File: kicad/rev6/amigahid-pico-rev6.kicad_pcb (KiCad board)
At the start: 2 copper layers, 100 x 80 mm, 115 parts, among them J1 A500 KBD OUT, J10 PS/2 KBD OUT, J11 DIN5 KBD IN, J12 PS/2 KBD IN, J13 USB-C AUX 5V, J2 DEBUG UART+SWD, J3 OLED I2C, J4 USB-A HOST, J7 SPARE GP28, J8 A500 KBD IN, J9 DIN5 KBD OUT, P1 DE9 MALE PORT 1, P2 DE9 MALE PORT 2, Q1 BSS138, Q10 BSS138, Q11 BSS138, Q12 BSS138, Q13 BSS138, Q14 BSS138, Q15 BSS138, Q16 BSS138, Q17 BSS138, Q18 BSS138, Q19 BSS138, Q2 BSS138, Q3 BSS138, Q4 BSS138, Q5 BSS138, Q6 BSS138, Q7 BSS138, Q8 BSS138, Q9 BSS138, U1 PicoW, U2 USBLC6-2SC6

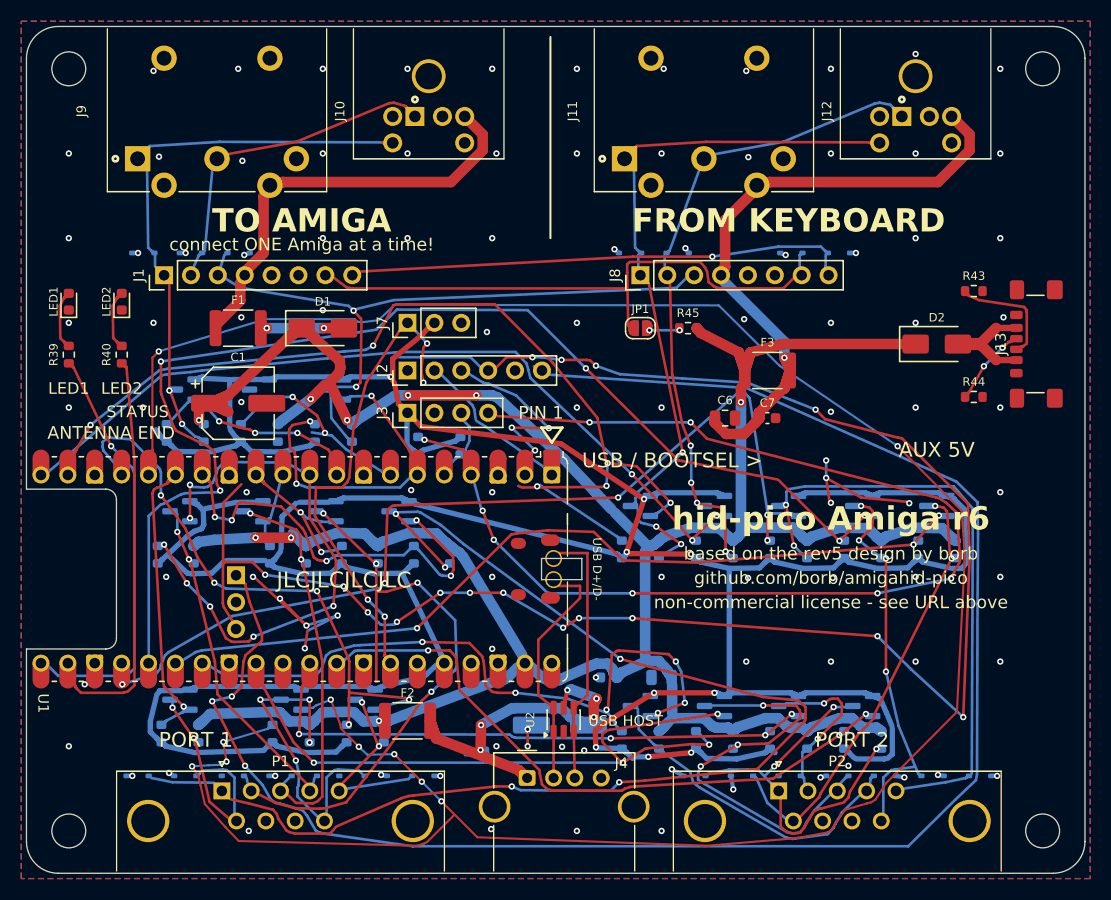
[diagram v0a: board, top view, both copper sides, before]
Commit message: kicad: drop the duplicated rev6 copper and trim the dead stubs
444 of the board's 2075 track and via objects were exact duplicates - same net, layer,
endpoints and width, stacked on top of each other by the successive re-lays.  they are
gone, which is most of the -4158 lines here.  they also explain why the last pass could
not clean up the dangling stubs: every stub had a copy of itself lying on it, so a
"does anything else touch this?" test always answered yes.

three stubs are trimmed back to their last live junction rather than deleted, because
each carries a junction partway along and deleting it - which is what the DRC line
suggests, since it reports the track's start, not its free end - orphans something:

  /cont1_h  F.Cu  11.15 -> 2.91 mm   (the remainder feeds the via on R12.2)
  /swdio    B.Cu   6.75 -> 0.29 mm
  /swdio    F.Cu   2.44 -> 0.29 mm

17 mm of unterminated copper gone.  the four sub-0.5 mm nubs left are what remains of
those tracks between their last junction and their end; they stay because trimming them
further disconnects the junction.

P2's shell tabs get the same solid zone connection P1's already have.  the two are the
same through-hole DE9 in the same pour and had no business soldering differently; the
split was accidental, not a decision.

CLAUDE.md gains a stated gate list for board commits - the old rule only covered
schematic changes, which is how a board with a failing checker reached the branch tip
unblocked - and records the pcbnew Save() footgun that strips netclass_patterns out of
the .kicad_pro.  .gitignore learns *.rpt.

what is left, honestly - all three measured this time, not assumed:

  /kbdata still will not close.  at the board's real rules (0.2 mm copper, 0.5 mm hole)
  there is no legal path at 0.02 mm resolution: Q2.3 and R4.2 share one free pocket
  whose only opening is a 0.267 mm wall on F.Cu at (15.42, 37.26), pinched between the
  /kbclock via at (14.70, 37.55) and the /SYS5V C1.1 -> R6.1 stub.  moving that stub
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
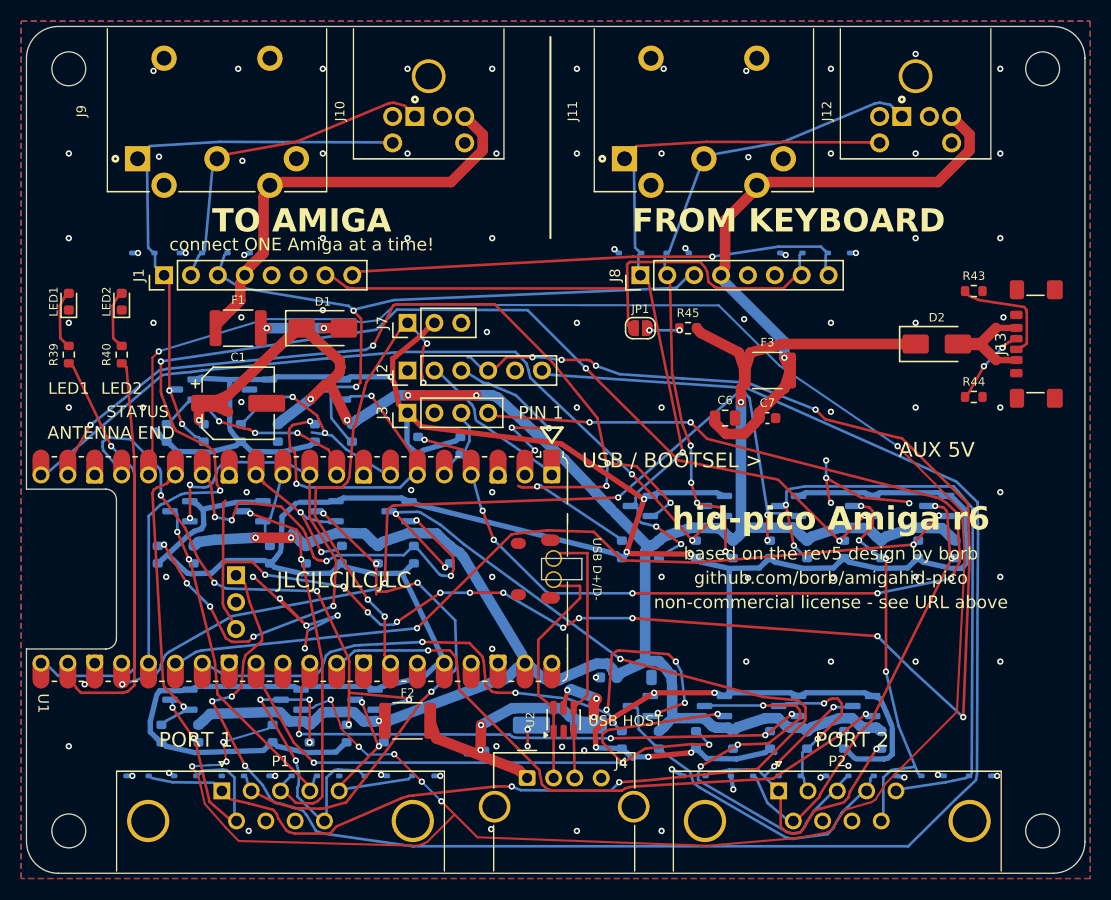
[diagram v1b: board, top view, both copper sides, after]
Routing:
- net +3V3: track 431.6 -> 349.6 mm
- net /SYS5V: track 315.3 -> 256.3 mm
- net /cont1_b1_lo: track 48.0 -> 29.4 mm
- net /cont1_h_lo: track 33.7 -> 16.7 mm
- net /gp28: track 57.8 -> 45.2 mm
- net /kbin_clk: track 78.5 -> 66.9 mm
- net /KBIN_5V: track 69.2 -> 58.6 mm
- net /swdio: track 170.7 -> 160.4 mm
- net /USBA_5V: track 40.0 -> 30.5 mm
- net /kbin_clk_lo: track 105.5 -> 96.0 mm
- net /kbclock: track 59.3 -> 50.5 mm
- net /kbreset_lo: track 38.4 -> 30.1 mm
- net /cont1_h: track 56.7 -> 48.4 mm
- net /cont1_b2_lo: track 235.6 -> 228.0 mm
- net /AMIGA_5V: track 47.5 -> 40.7 mm
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
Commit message: kicad: move the esd clamps off the de9 pins and close /kbdata
all three gates are green after this: DRC 0 violations / 0 unconnected, check_rev6_pcb
32/32, check_rev6_netlist 356/356.

the clamp rows under P1 and P2 move 0.6 mm north.  they were 0.395 mm from the DE9
through-hole pads - under JLCPCB's 0.4 mm solder-mask dam, and with no room to get an
iron onto the DE9 pins - and six of those pads' mask openings clipped a clamp body
outline, which is where the 14 silk_over_copper lines came from.  the copper gap is now
0.995 mm and the silk clears the mask by 0.295 mm.  the whole row moves, not just the six
offenders, so it is still a straight row.

every clamp now owns a ground via with a 0.4-1.1 mm stub to it.  D13 and D15 had none at
all - the checker called them stranded - and D24 and D27 were only saved by the pour
happening to reach them.  ten of the fourteen keep the via they already had, because
those spots are known clean.

/kbdata is closed.  its channel is built exactly like /kbclock's and /kbreset's - shifter
source pad on the Q row, pull-up on the R row, and the _lo diagonal between them, so the
pair has to cross - and the other two cross on F.Cu.  /kbdata could not, because the
SYS5V front rail lay across the only place to do it.  the rail is re-laid west of the
column and /kbdata crosses in 4.9 mm; the net is 57.6 mm and 2 vias, against the 103 mm
and 8 vias a router given the old rail produces.  C1 does not move: rotating it 90 degrees
was tried first and its courtyard is 9.39 mm tall against the 9.28 mm between F1 and U1.

every ground pour region is now part of the plane.  five clamp ground pads sat on islands
of their own - a pour-only ground makes such a region a dead node, and DRC reports it only
as an anonymous zone-to-zone line that names no part.  three are tied by a via.  the two
that were walled in by the fan-out are reached by ripping one neighbouring net, taking a
0.4 mm ground bridge out through the hole, and re-laying that net; a wall w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
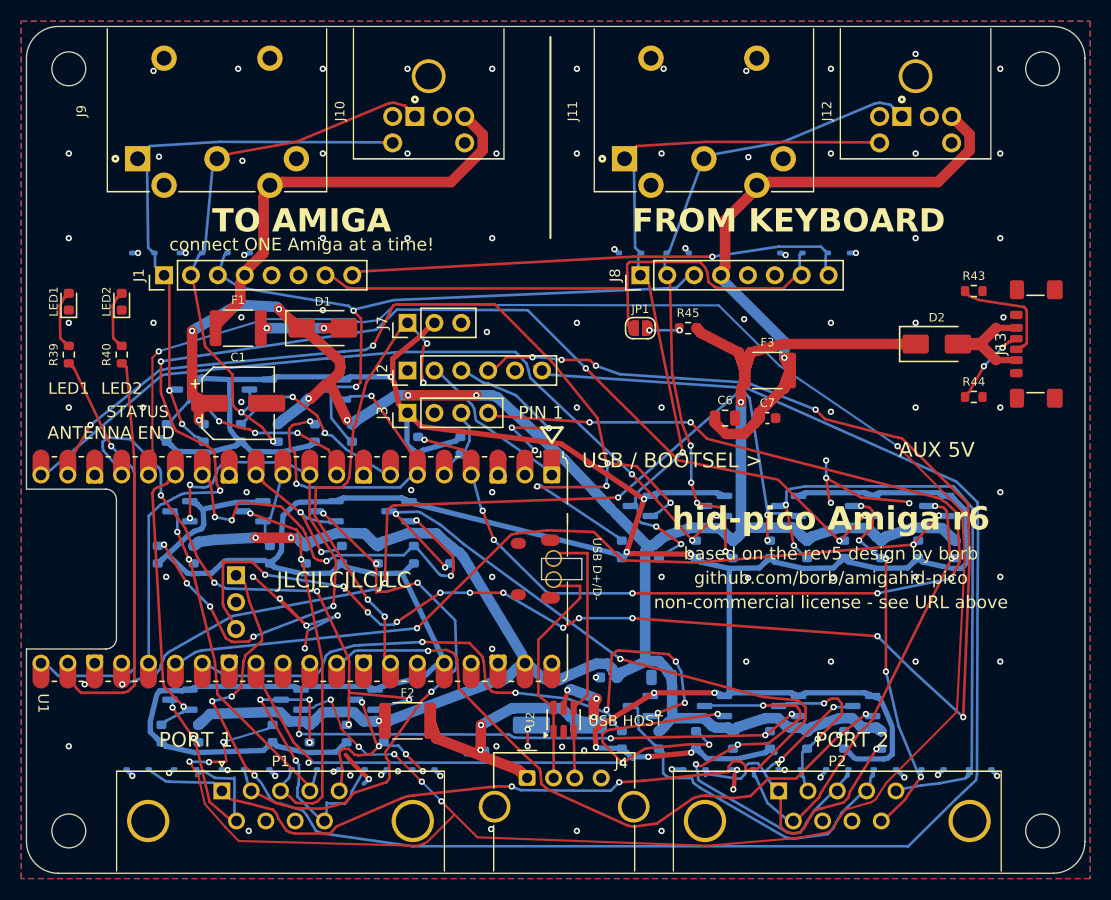
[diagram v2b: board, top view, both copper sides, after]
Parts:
- moved D13 0.60 mm to (28.5, 70.2)
- moved D14 0.60 mm to (24.0, 70.2)
- moved D15 0.60 mm to (19.5, 70.2)
- moved D16 0.60 mm to (10.5, 70.2)
- moved D17 0.60 mm to (15.0, 70.2)
- moved D18 0.60 mm to (33.0, 70.2)
- moved D19 0.60 mm to (37.5, 70.2)
- moved D22 0.60 mm to (90.1, 70.2)
- moved D23 0.60 mm to (85.6, 70.2)
- moved D24 0.60 mm to (67.6, 70.2)
- moved D25 0.60 mm to (81.1, 70.2)
- moved D26 0.60 mm to (76.6, 70.2)
- moved D27 0.60 mm to (72.1, 70.2)
- moved D28 0.60 mm to (63.1, 70.2)
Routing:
- net +3V3: track 349.6 -> 433.7 mm
- net /SYS5V: track 256.3 -> 306.3 mm, vias 9 -> 11
- net /kbdata: track 28.4 -> 57.6 mm, vias 0 -> 2
- net /KBIN_5V: track 58.6 -> 76.5 mm
- net /gp28: track 45.2 -> 59.4 mm
- net /kbclock: track 50.5 -> 61.8 mm
- net /USBA_5V: track 30.5 -> 40.0 mm
- net /cont1_b2_lo: track 228.0 -> 236.2 mm
- net GND: track 43.2 -> 50.9 mm, vias 103 -> 109
- net /swdio: track 160.4 -> 153.0 mm
- net /AMIGA_5V: track 40.7 -> 47.5 mm
- net /cont2_hq: track 29.1 -> 35.2 mm
- net /kbdata_lo: track 19.3 -> 25.1 mm
- net /cont2_b3: track 57.5 -> 63.0 mm
- net /usb_cc2: track 7.49 -> 13.1 mm
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
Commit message: kicad: widen the power via transitions and shorten the decoupling returns
all three gates stay green: DRC 0 violations / 0 unconnected, check_rev6_pcb 32/32,
check_rev6_netlist 356/356.

every power layer transition was a single 0.6/0.3 via and the input current crosses two
of them in series.  the Power netclass asks for 0.9/0.5 and nothing was using it, so the
three transitions with the room are widened to it, and 22 more vias go in beside the rest
- three per transition where they fit - tied on both layers by 0.8 mm links, which is what
F2 wants of a power segment.  /AMIGA_5V_FUSED, /KBIN_5V and the two busiest /USBA_5V and
/SYS5V transitions now carry three barrels each instead of one.

C2, C6 and C7 had their ground pad 5.3-7.0 mm from the nearest ground via, so their
return current went the long way through the pour before it found a way to the other
layer.  each gets a via of its own within 0.7 mm.  C1's first placement put the via
0.45 mm off Q2's source pad - a hole-clearance error the clearance model missed, because
it only checked a via's hole against pads that have holes of their own - and it is
re-sited 0.70 mm out on the other side.

J4 is centred.  the channel between the DE9 hoods is x 39.955 to 60.645 and the USB-A sat
0.50 mm east of the middle of it; it now sits in the middle.  the five stubs on its pads
came with it and the two nets its pads landed on are re-laid.

the ground stitcher had to move two more islands: J3's ground pin and J7's, walled in by
/uart_tx and /i2c_sda.  a wall pair is ripped, the ground bridge laid, and both nets put
back - single walls could not be re-laid once the bridge had the lane.

/i2c_sda's route stopped 0.12 mm short of U1 pin 4: the router models a roundrect pad as a
plain rectangle and will end a route in a corner the real pad does not occupy.  the end is
carried onto the pad.  welding every end that lands near a pad fixes that class of thing
but adds a thousand stubs and 760 mm of copper; only the two ends KiCad 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
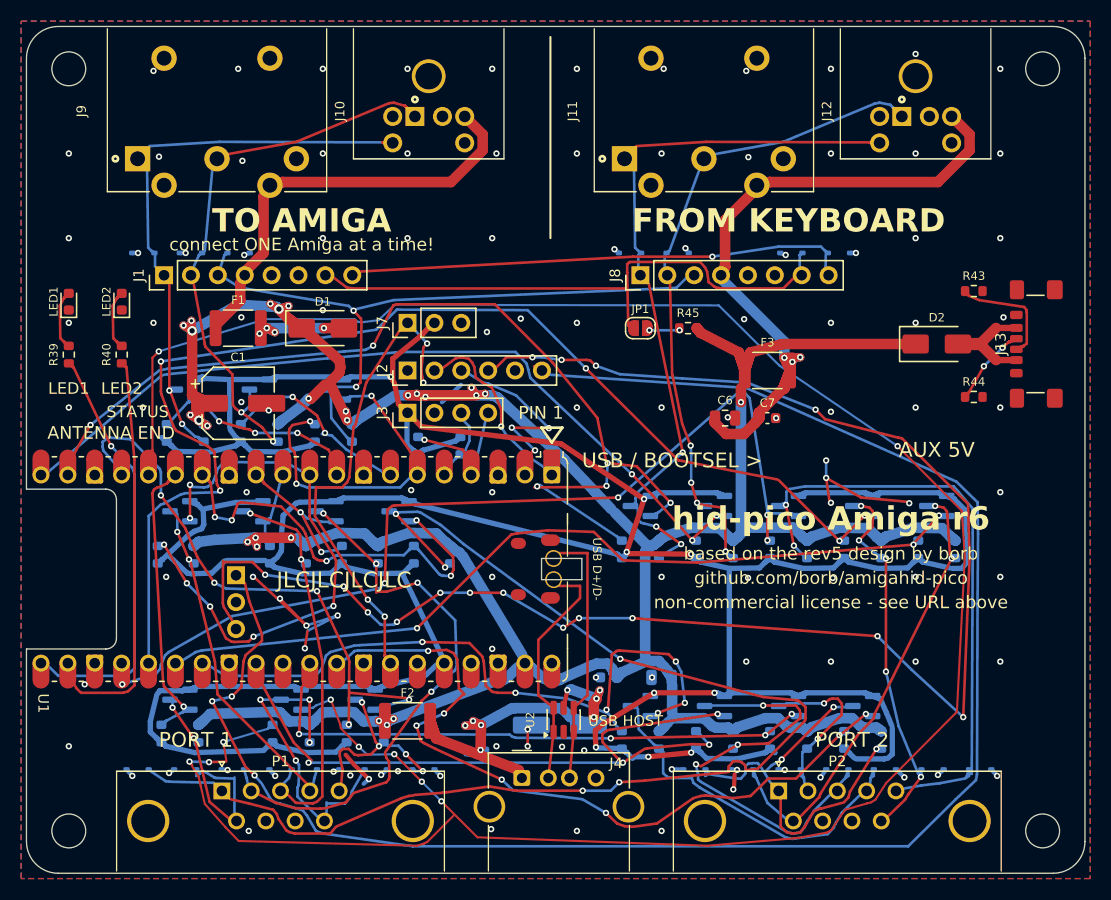
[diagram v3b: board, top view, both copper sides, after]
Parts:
- moved J4 0.50 mm to (46.8, 71.0)
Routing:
- net /i2c_sda: track 111.1 -> 12.0 mm, vias 8 -> 1
- net /SYS5V: track 306.3 -> 353.2 mm, vias 11 -> 26
- net /cont2_v_lo: track 61.6 -> 69.5 mm, vias 3 -> 7
- net /KBIN_5V: track 76.5 -> 81.2 mm, vias 1 -> 3
- net GND: track 50.9 -> 55.4 mm, vias 109 -> 114
- net /USBA_5V: track 40.0 -> 43.9 mm, vias 5 -> 8
- net /AMIGA_5V_FUSED: track 7.86 -> 11.3 mm, vias 2 -> 4
- net /uart_tx: track 16.3 -> 19.2 mm, vias 0 -> 1
- net /cont1_b3: track 16.5 -> 19.1 mm

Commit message: kicad: give the usb pair a ground reference on the other layer
all three gates stay green: DRC 0 violations / 0 unconnected, check_rev6_pcb 32/32,
check_rev6_netlist 356/356.

only 11-16% of usb_dp/usb_dm had ground under them on the other layer.  the corridor
beneath the pair is the board's main east-west channel on B.Cu - +3V3, SYS5V, USBA_5V,
swdio and five of the _lo nets all cross it - so the pour cannot get in, and re-pathing
the pair means moving that channel.

instead the pair gets a ground shadow: 10.1 mm of track on the other layer following it,
laid in the stretches that are legal and stitched to the plane at the end of each stretch
with 7 vias.  the return current now has somewhere to go directly under the signal rather
than round the break.  coverage is 51% and 55%.

the shadow's long run alongside the antenna cut-out is 0.40 mm rather than 0.50 mm wide:
the cut-out is an internal Edge.Cuts chain and counts for copper_edge_clearance the same
as the outline, which the clearance model did not know until now.  at 0.50 mm it cleared
by 0.28 mm against a 0.30 mm rule.

copper: 3887 -> 3904 mm, 332 -> 339 vias.
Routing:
- net GND: track 55.4 -> 71.7 mm, vias 114 -> 121
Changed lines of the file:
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@@
+	)
+	(via
+		(at 51.389777 53.727982)
+		(size 0.6)
+		(drill 0.3)
+		(layers "F.Cu" "B.Cu")
+		(net "GND")
 	)
 	(via
@@
 	)
 	(via
+		(at 53.832683 50.341523)
+		(size 0.6)
+		(drill 0.3)
+		(layers "F.Cu" "B.Cu")
+		(net "GND")
+	)
+	(via
 		(at 11 36)
 		(size 0.6)
@@
 	)
 	(via
+		(at 47.582126 57.597345)
+		(size 0.6)
+		(drill 0.3)
+		(layers "F.Cu" "B.Cu")
+		(net "GND")
+	)
+	(via
 		(at 55.548676 21.046467)
 		(size 0.6)
@@
 	)
 	(via
+		(at 53.826219 55.000347)
+		(size 0.6)
+		(drill 0.3)
+		(layers "F.Cu" "B.Cu")
+		(net "GND")
+	)
+	(via
 		(at 39.1 70.8)
 		(size 0.6)
@@
 	)
 	(via
+		(at 49.192683 58.281523)
+		(size 0.6)
+		(drill 0.3)
+		(layers "F.Cu" "B.Cu")
+		(net "GND")
+	)
+	(via
 		(at 92 12)
 		(size 0.6)
@@
 	)
 	(via
+		(at 50.597621 54.516233)
+		(size 0.6)
+		(drill 0.3)
+		(layers "F.Cu" "B.Cu")
+		(net "GND")
+	)
+	(via
 		(at 20.8 44)
 		(size 0.6)
@@
 	(via
 		(at 60.2 4)
+		(size 0.6)
+		(drill 0.3)
+		(layers "F.Cu" "B.Cu")
+		(net "GND")
+	)
+	(via
+		(at 49.920397 57.565749)
 		(size 0.6)
 		(drill 0.3)
@@
 	)
 	(segment
+		(start 53 50)
+		(end 53 55.2)
+		(width 0.4)
+		(layer "B.Cu")
+		(net "GND")
+	)
+	(segment
 		(start 29.55 70.2)
 		(end 29.012558 70.399605)
 		(width 0.4)
+		(layer "B.Cu")
+		(net "GND")
+	)
+	(segment
+		(start 49.424865 56.875135)
+		(end 48.36 57.94)
+		(width 0.5)
+		(layer "B.Cu")
+		(net "GND")
+	)
+	(segment
+		(start 49.424865 56.875135)
+		(end 49.920397 57.565749)
+		(width 0.5)
 		(layer "B.Cu")
 		(net "GND")
@@
 	)
 	(segment
+		(start 48.36 57.94)
+		(end 48.36 59.643238)
+		(width 0.5)
+		(layer "B.Cu")
+		(net "GND")
+	)
+	(segment
+		(start 48.36 57.94)
+		(end 47.582126 57.597345)
+		(width 0.5)
+		(layer "B.Cu")
+		(net "GND")
+	)
+	(segment
 		(start 9.45 70.2)
 		(end 10 70.8)
@@
 	)
 	(segment
+		(start 51.093153 55.206847)
+		(end 50.597621 54.516233)
+		(width 0.5)
+		(layer "B.Cu")
+		(net "GND")
+	)
+	(segment
 		(start 13.95 70.2)
 		(end 13.473686 70.525)
@@
 	)
 	(segment
+		(start 52.3 54)
+		(end 51.093153 55.206847)
+		(width 0.5)
+		(layer "B.Cu")
+		(net "GND")
+	)
+	(segment
 		(start 62.57 21.4)
 		(end 62.254533 20.949466)
@@
 	)
 	(segment
+		(start 53 55.2)
+		(end 53.826219 55.000347)
+		(width 0.5)
+		(layer "B.Cu")
+		(net "GND")
+	)
+	(segment
 		(start 40.15 34.7)
 		(end 41.05 33.85)
 		(width 0.4)
+		(layer "B.Cu")
+		(net "GND")
+	)
+	(segment
+		(start 48.36 57.94)
+		(end 49.192683 58.281523)
+		(width 0.5)
 		(layer "B.Cu")
 		(net "GND")
@@
 	)
 	(segment
+		(start 52.3 54)
+		(end 51.389777 53.727982)
+		(width 0.5)
+		(layer "B.Cu")
+		(net "GND")
+	)
+	(segment
 		(start 34.05 70.2)
 		(end 33.508356 70.704494)
@@
 		(layer "B.Cu")
 		(net "GND")
+	)
+	(segment
+		(start 53 50)
+		(end 53.832683 50.341523)
+		(width 0.5)
+		(layer "B.Cu")
+		(net "GND")
